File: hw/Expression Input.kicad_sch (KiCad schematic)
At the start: 10 parts, among them J6 Exp, J7 Exp Connector, U7 NE5532

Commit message: huge schematic rework
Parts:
- removed D4, D5: B5819W SL, Diode_SMD:D_SOD-123, symbol Device:D_Schottky
- removed R17, R18: 1k, Resistor_SMD:R_0603_1608Metric, symbol Device:R
- removed R19: 2M, Resistor_SMD:R_0603_1608Metric, symbol Device:R
- added R10, R24: 10k, symbol Device:R
- added R16, R20: 100k, symbol Device:R
- added TP6: VS, TestPoint:TestPoint_Pad_D2.0mm, symbol Connector:TestPoint
- TP8: value EXP -> VR
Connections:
- net +3.3VA: now also R24.1; no longer U7.3 (+)
- net GND: now also R10.2; no longer J6.S, J7.1 (Pin_1)
- net EXP_R: now reaches J6.R, J7.2 (Pin_2)
- net EXP_R: now also U7.5 (+), R16.1, R20.2
- net EXP_T: now reaches J6.T, J7.3 (Pin_3)
- net EXP_T: now also U7.3 (+), R20.1, R24.2
- net EXP_IN renamed VR
- net VR: now also TP8.1
- net EXP_REF renamed VS
- net VS: now also TP6.1
- removed net EXP_SENSE: TP8.1, U7.5 (+)
- new net EXP_S: J6.S, J7.1 (Pin_1), R10.1, R16.2
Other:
- moved on the sheet: C23, J6, J7, TP8, U7A, U7B, U7C

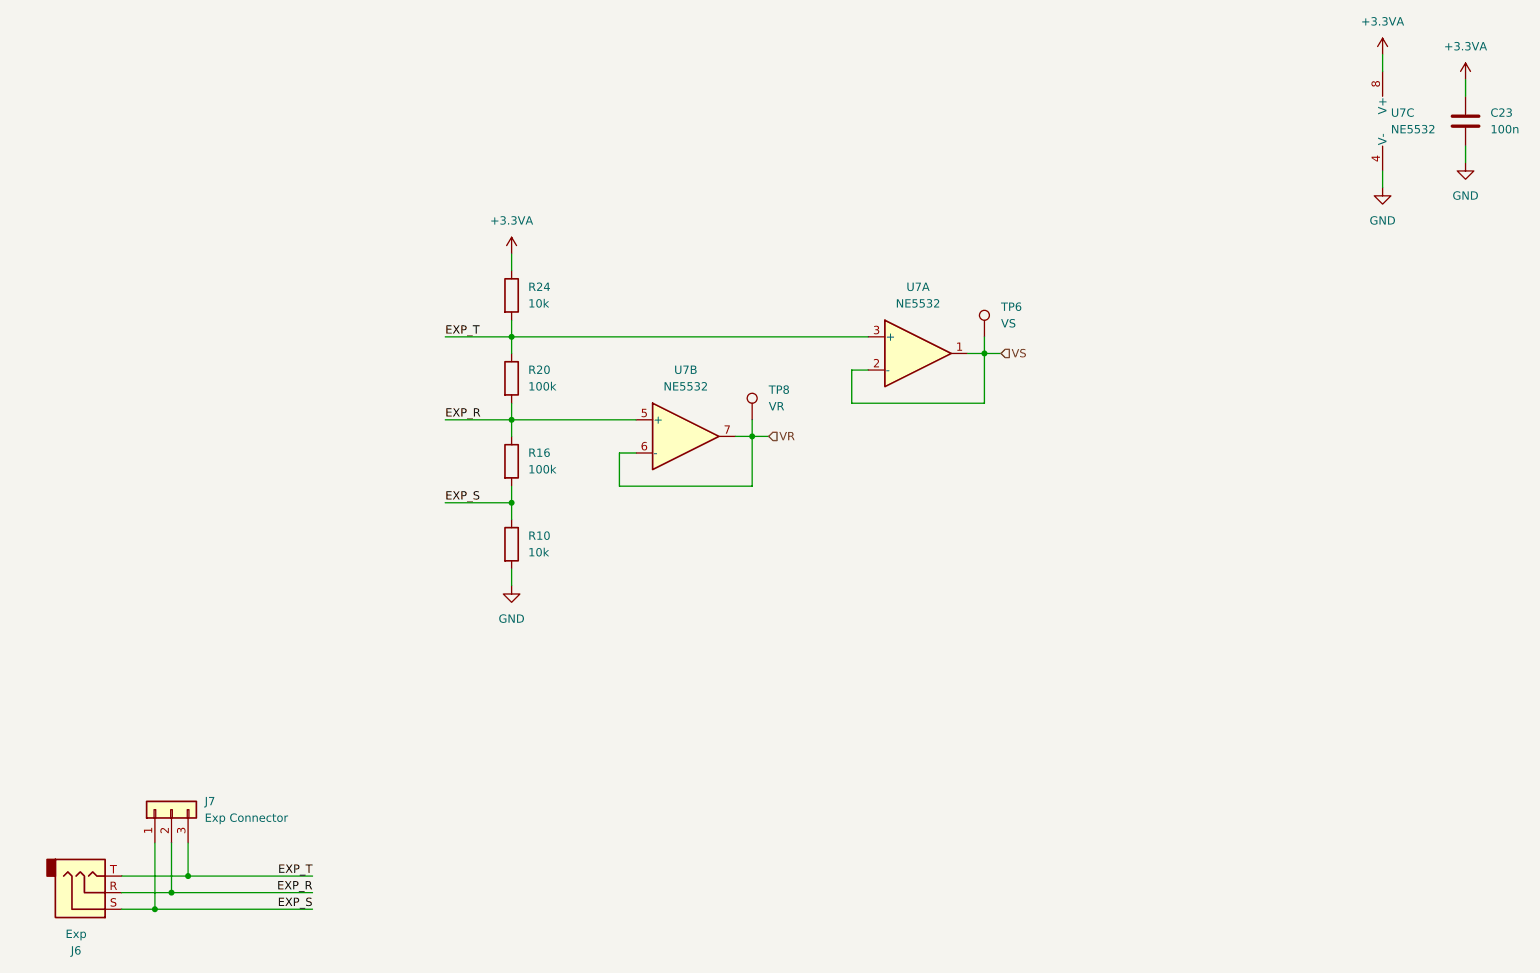
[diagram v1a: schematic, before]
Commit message: added new pcb design, ERC errors not fixed yet
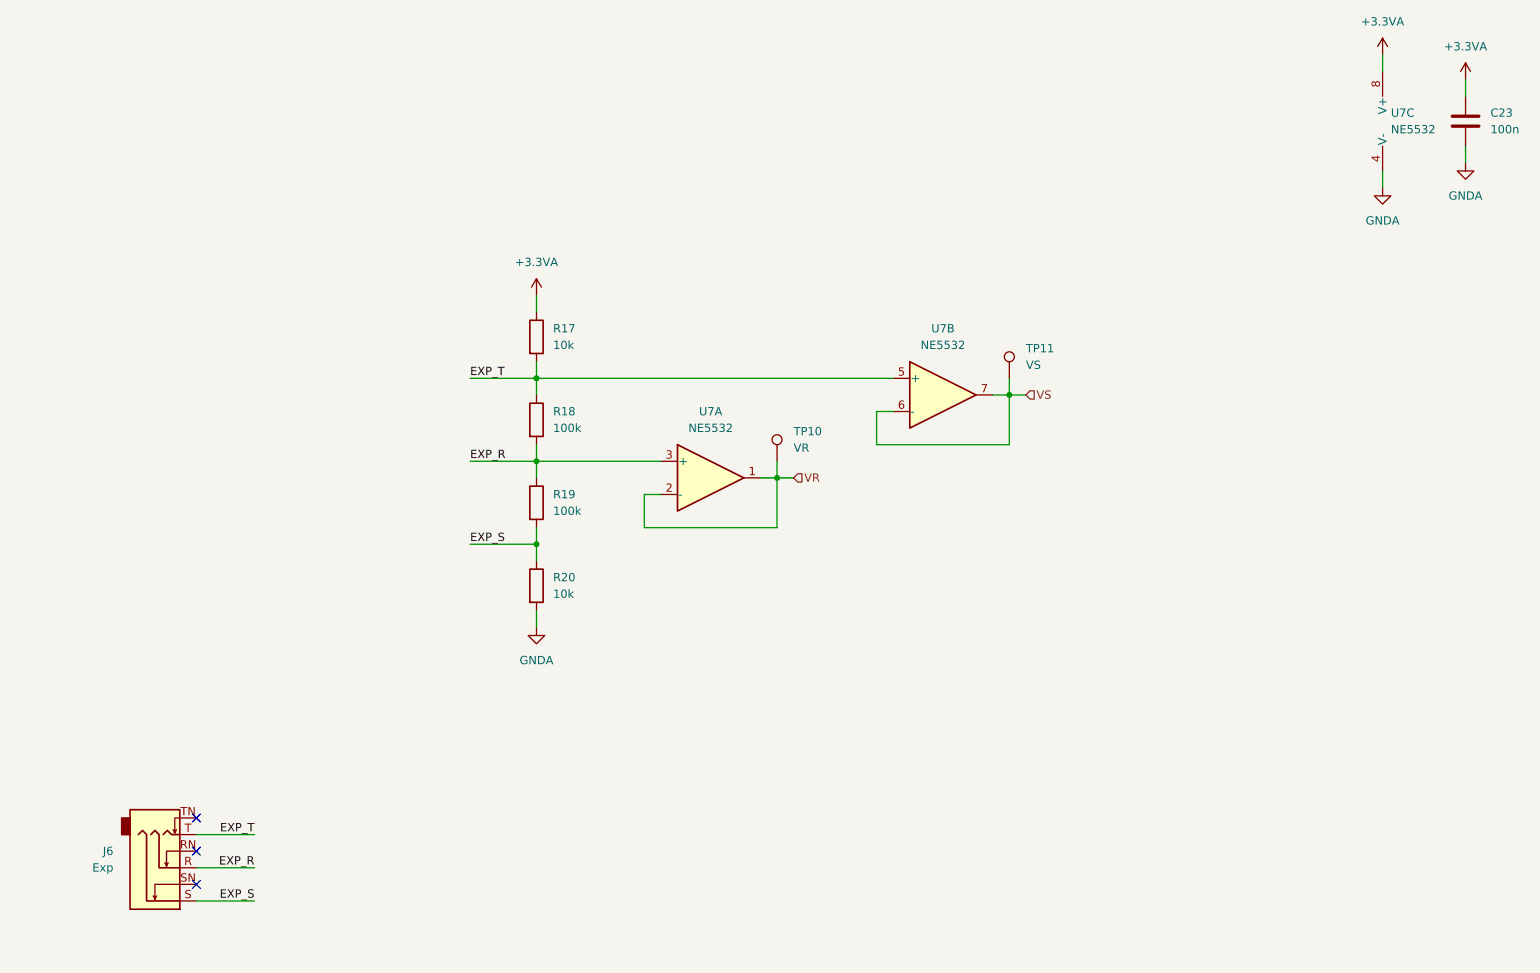
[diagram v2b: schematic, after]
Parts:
- removed J7: Exp Connector, Connector_PinHeader_2.54mm:PinHeader_1x03_P2.54mm_Vertical, symbol Connector_Generic:Conn_01x03
- C23: LCSC (none) -> C14663
- J6: footprint (none) -> Connector_Audio:Jack_6.35mm_Neutrik_NMJ6HFD4_Horizontal; symbol Connector_Audio:AudioJack3 -> Connector_Audio:AudioJack3_Switch; now in the parts list
- R17: renamed from R24; footprint (none) -> Resistor_SMD:R_0603_1608Metric; LCSC (none) -> C25804
- R18: renamed from R20; footprint (none) -> Resistor_SMD:R_0603_1608Metric
- R19: renamed from R16; footprint (none) -> Resistor_SMD:R_0603_1608Metric
- R20: renamed from R10; footprint (none) -> Resistor_SMD:R_0603_1608Metric; LCSC (none) -> C25804
- U7: LCSC (none) -> C7426
- renumbered TP8 to TP10, TP6 to TP11
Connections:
- net EXP_R: now also U7.3 (+); no longer U7.5 (+)
- net EXP_T: now also U7.5 (+); no longer U7.3 (+)
- net VR: now also U7.1, U7.2 (-); no longer U7.6 (-), U7.7
- net VS: now also U7.6 (-), U7.7; no longer U7.1, U7.2 (-)
- net GND renamed GNDA
- no-connect marks 0 -> 3
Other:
- moved on the sheet: R17, R18, R19, R20, TP10, TP11, U7A, U7B

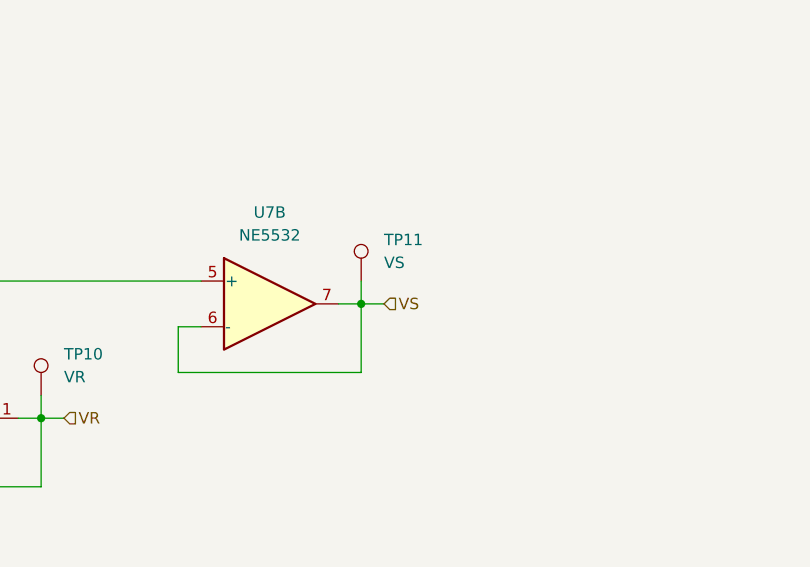
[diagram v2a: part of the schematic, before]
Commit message: fixed input range issue
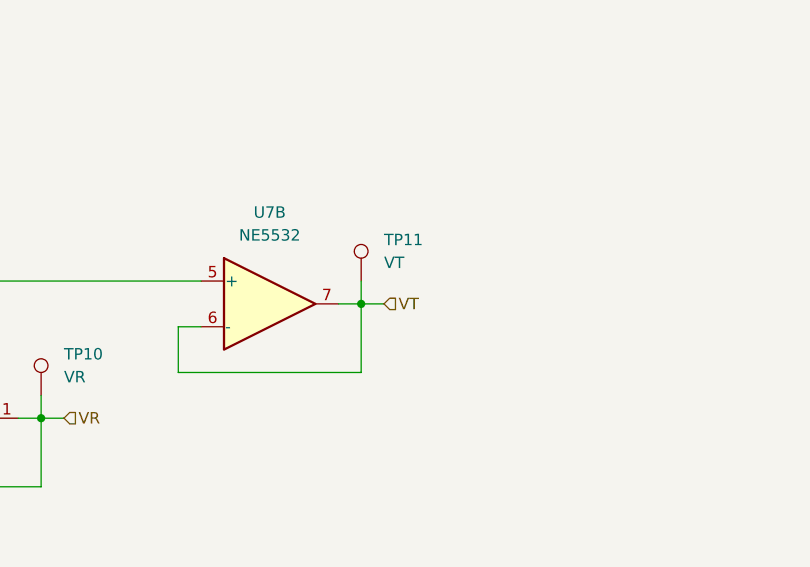
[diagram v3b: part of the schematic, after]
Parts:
- TP11: value VS -> VT
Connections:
- net VS renamed VT
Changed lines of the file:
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@@
 		)
 	)
-	(hierarchical_label "VS"
+	(hierarchical_label "VT"
 		(shape input)
 		(at 184.15 91.44 0)
@@
 			)
 		)
-		(property "Value" "VS"
+		(property "Value" "VT"
 			(at 184.15 86.8679 0)
 			(effects
